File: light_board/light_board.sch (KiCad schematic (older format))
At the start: 16 parts, among them J1 CONN_01X02, J2 Led_Connector, J3 Power_Connector, Q1 FDC658AP, U1 LM3409MY

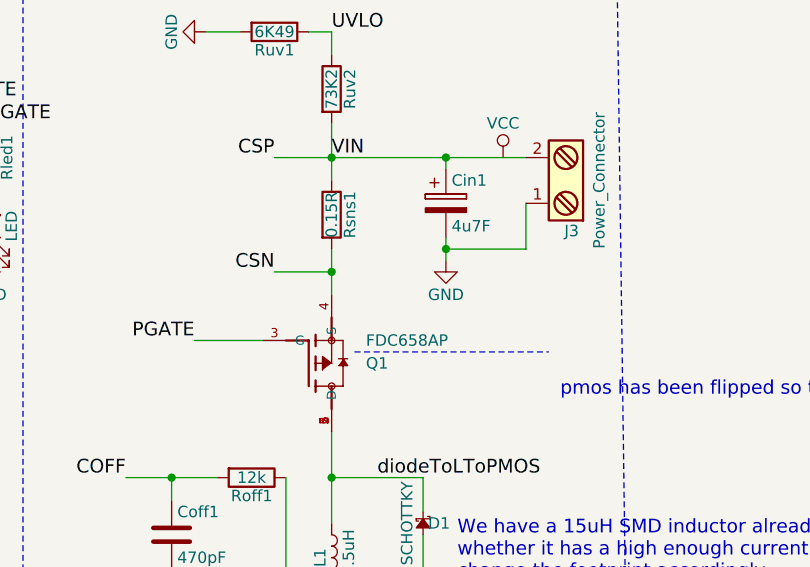
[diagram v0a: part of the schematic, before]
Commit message: light board finished - added ground plane and thick tracks
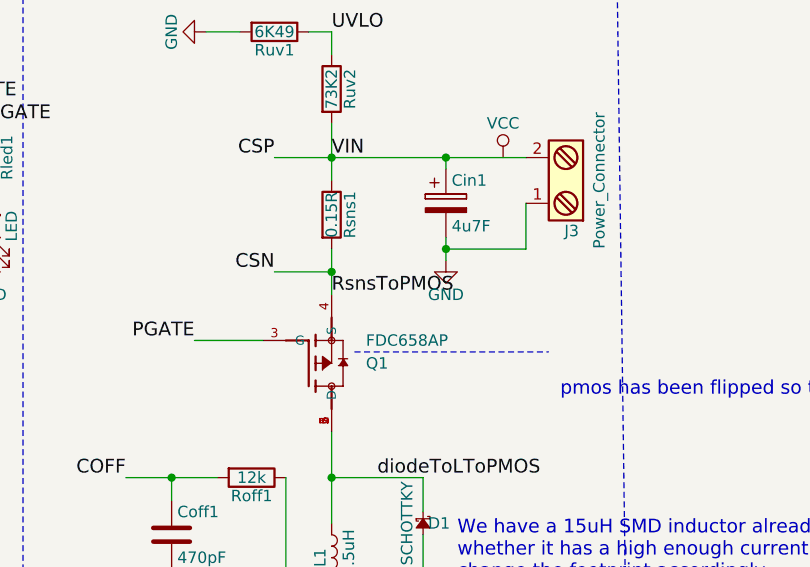
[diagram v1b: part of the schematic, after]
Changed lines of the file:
@@
 Text Label 6750 2900 0    60   ~ 0
 PGATE
+Text Label 8250 3650 0    60   ~ 0
+RsnsToPMOS
 $EndSCHEMATC
